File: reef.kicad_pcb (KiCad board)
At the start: 2 copper layers, 87 parts, among them J1 nice!view sockets, J2 battery connector, SW0 B3U-1000P[], SW1 PCM12SMTR, U1 nice_nano, U2 TRRS, U3 TRRS

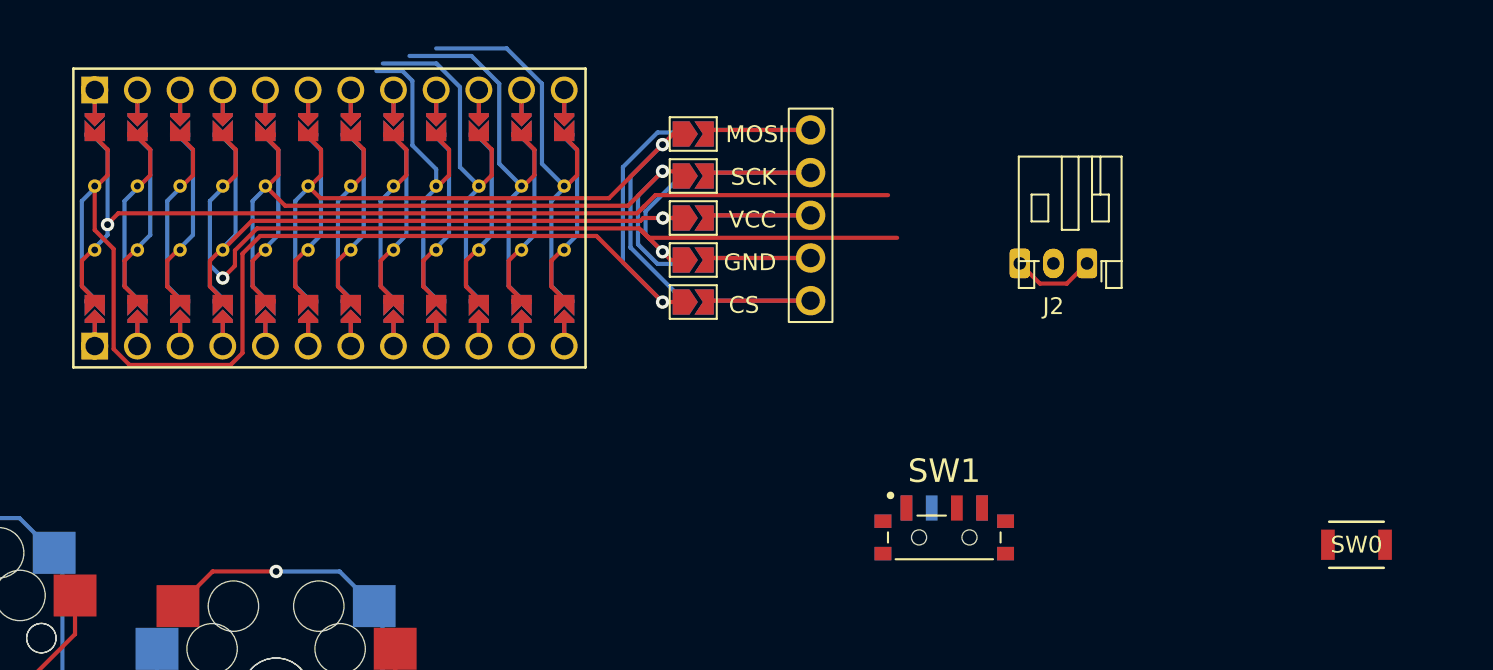
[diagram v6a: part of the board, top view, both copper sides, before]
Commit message: Reset, Power, Battery
routed reset switch, power switch, battery connector
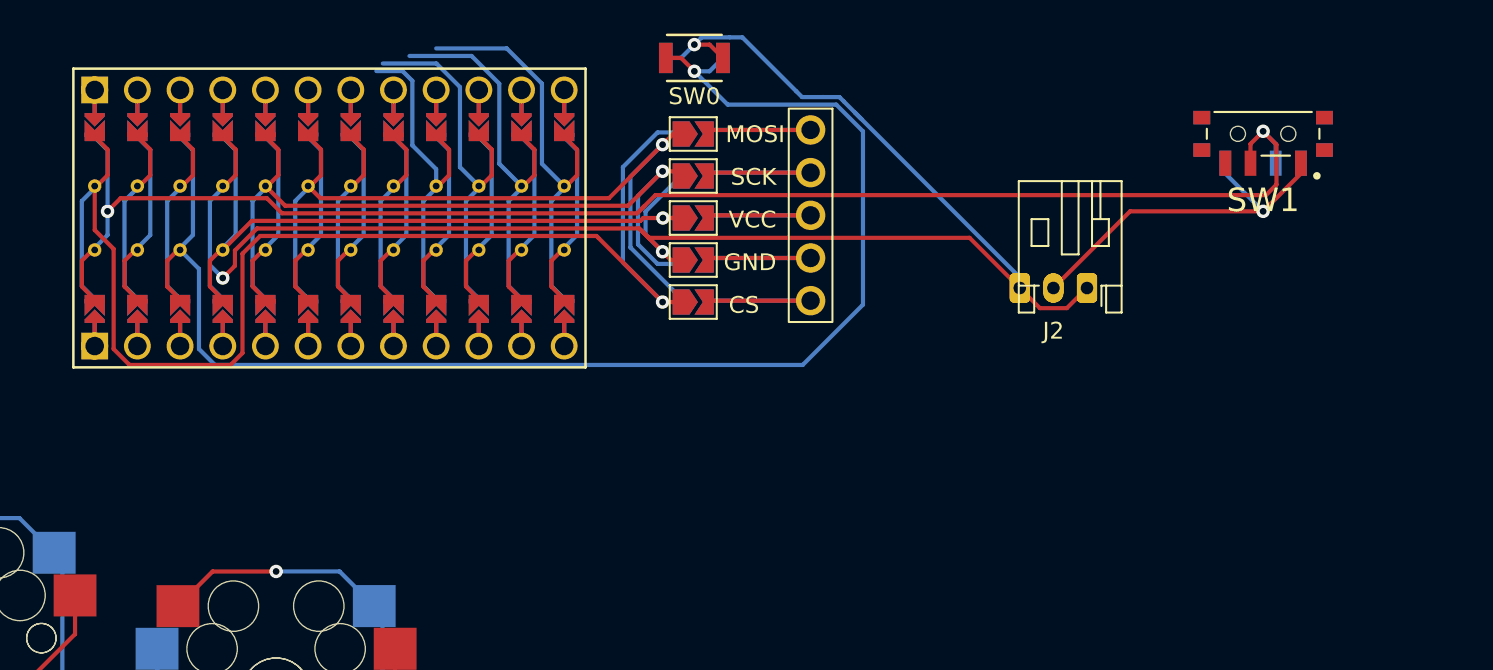
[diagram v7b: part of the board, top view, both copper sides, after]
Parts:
- SW0: moved to B.Cu
- moved SW0 48.9 mm to (167.0, 28.2)
- moved SW1 33.2 mm to (200.8, 31.1), turned to 180 degrees
- moved J2 1.46 mm to (188.3, 38.9)
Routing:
- net rst: track 0.00 -> 73.6 mm, vias 0 -> 1
- net gnd: track 57.1 -> 96.3 mm, vias 2 -> 3
- net bat+: track 47.8 -> 79.5 mm, vias 1 -> 2
- net bat_sw+: track 0.00 -> 22.0 mm, vias 0 -> 1

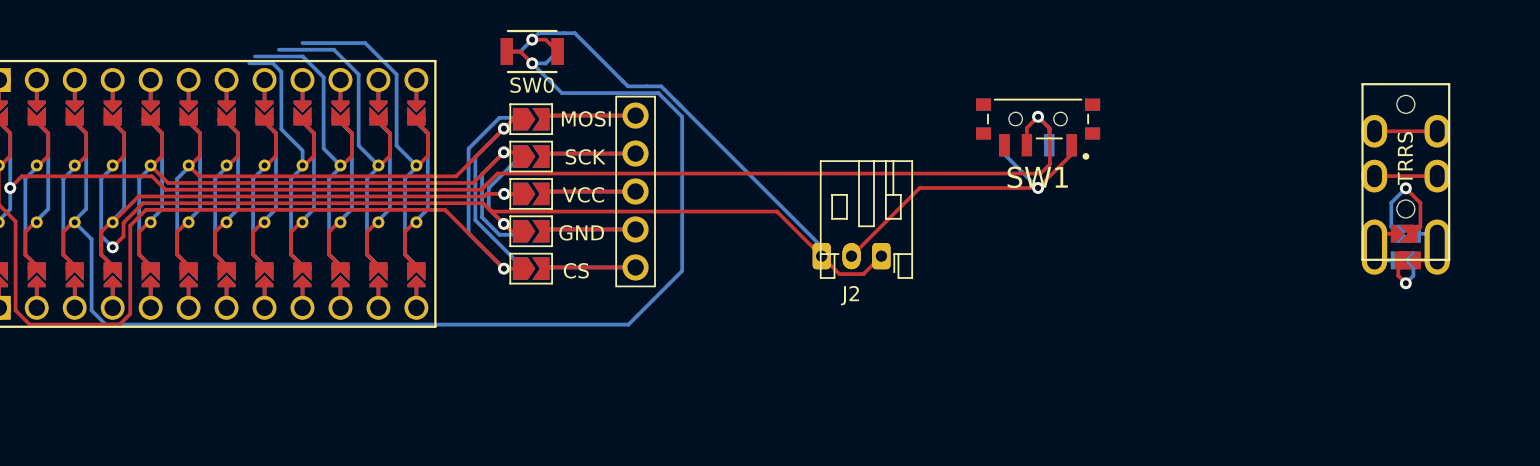
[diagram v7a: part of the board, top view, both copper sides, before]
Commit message: Ports and Switches
rerouted reset switch, routed trrs connector. all switches and ports should now be routed
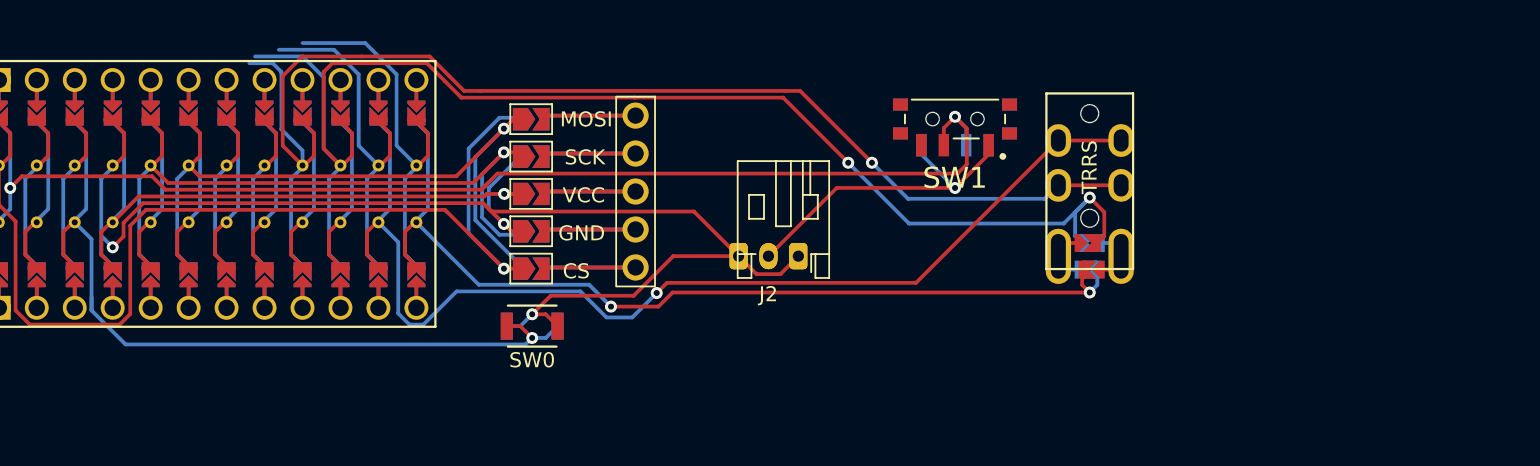
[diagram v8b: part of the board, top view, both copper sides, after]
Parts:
- moved U2 21.2 mm to (204.3, 30.8)
- moved SW0 18.4 mm to (167.0, 46.5)
- moved J2 5.56 mm to (182.8, 38.9)
- moved SW1 5.56 mm to (195.3, 31.1)
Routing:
- net row_1: track 156.1 -> 219.4 mm, vias 7 -> 8
- net row_0: track 145.1 -> 208.4 mm, vias 6 -> 7
- net col_6: track 4.20 -> 61.9 mm, vias 0 -> 1
- net col_7: track 3.48 -> 51.3 mm, vias 1 -> 2
- net rst: track 73.6 -> 41.9 mm
- net gnd: track 96.3 -> 79.4 mm
- net bat+: track 79.5 -> 73.9 mm
